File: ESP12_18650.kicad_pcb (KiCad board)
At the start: 2 copper layers, 77.7 x 20.5 mm, 28 parts, among them J1 Conn_02x06_Counter_Clockwise, J10 Conn_01x06_Male, J11 Conn_01x06_Male, J12 Conn_01x06_Male, J13 Conn_01x06_Male, J14 Conn_01x06_Male, J15 Conn_01x06_Male, J16 Conn_01x06_Male, J17 Conn_01x14_Male, J2 Conn_01x14_Male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

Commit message: Add +/- battery pole labels
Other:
- board text added: "+"
- board text added: "-"
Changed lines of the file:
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@@
     (effects (font (size 1 1) (thickness 0.25)) (justify mirror))
+  )
+  (gr_text "-" (at 135.986316 65.996077) (layer "B.SilkS")
+    (effects (font (size 2 2) (thickness 0.5)) (justify mirror))
   )
   (gr_text "3V3" (at 67.818 78.74) (layer "B.SilkS")
@@
     (effects (font (size 1 1) (thickness 0.25)) (justify mirror))
   )
+  (gr_text "+" (at 64 66) (layer "B.SilkS")
+    (effects (font (size 2 2) (thickness 0.5)) (justify mirror))
+  )
   (gr_text "15" (at 115.2 68.2) (layer "F.SilkS")
     (effects (font (size 1 1) (thickness 0.25)))
+  )
+  (gr_text "-" (at 136 66) (layer "F.SilkS")
+    (effects (font (size 2 2) (thickness 0.5)))
   )
   (gr_text "16" (at 67.818 76.2) (layer "F.SilkS")
@@
     (effects (font (size 1 1) (thickness 0.25)))
   )
+  (gr_text "+" (at 64 66) (layer "F.SilkS")
+    (effects (font (size 2 2) (thickness 0.5)))
+  )
   (gr_text "1" (at 106.5 63.5) (layer "F.SilkS")

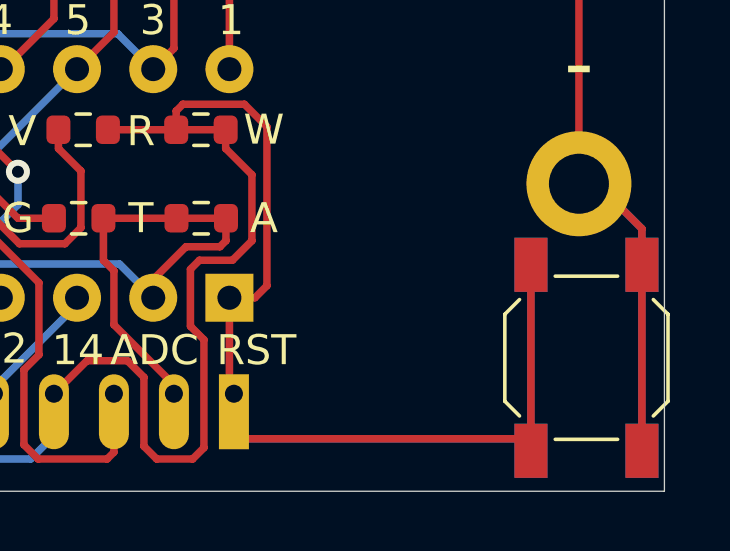
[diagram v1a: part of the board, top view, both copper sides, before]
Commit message: Flip battery holder (looks better in 3D), and fix/avoid CRC errors
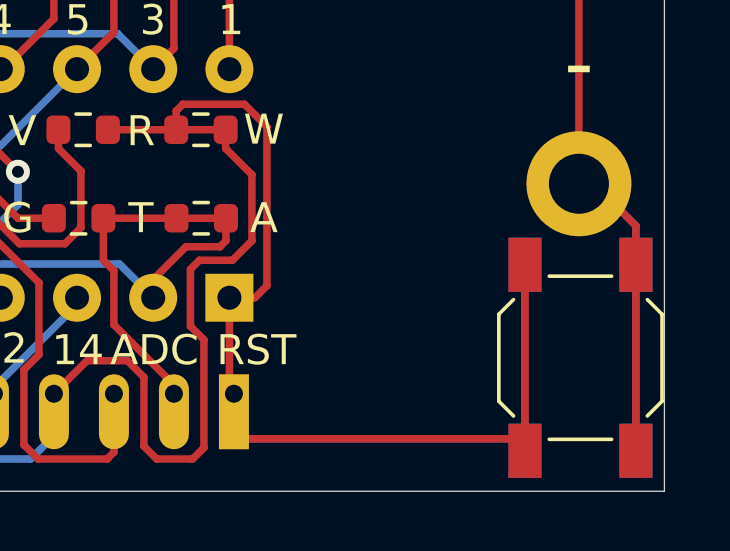
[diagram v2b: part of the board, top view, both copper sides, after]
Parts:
- BT1: moved to F.Cu
- moved SW1 0.20 mm to (136.1, 75.8)
- moved SW2 0.20 mm to (136.1, 75.8)
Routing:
- net GND: track 111.6 -> 112.1 mm
